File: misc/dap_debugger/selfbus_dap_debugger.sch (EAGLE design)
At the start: 60 parts, among them CON1 MICRO-B_U254-051N-4BH806, CON2 SHF-105-01-X-D-TH, CON3 SHF-105-01-X-D-TH, CON4 SAMTEC-LTMM-105-02-T-D, IC1 74LVC1T45GW, IC2 74LVC2G07GV, IC3 74LVC2T45DC, IC4 74LVC2T45DC, SW1 BOOT, SW2 RESET, SW3 XKB7070-Z, U1 STM32F042FX, U2 AP2112K-3.3TRG1, U3 AP2331TDW

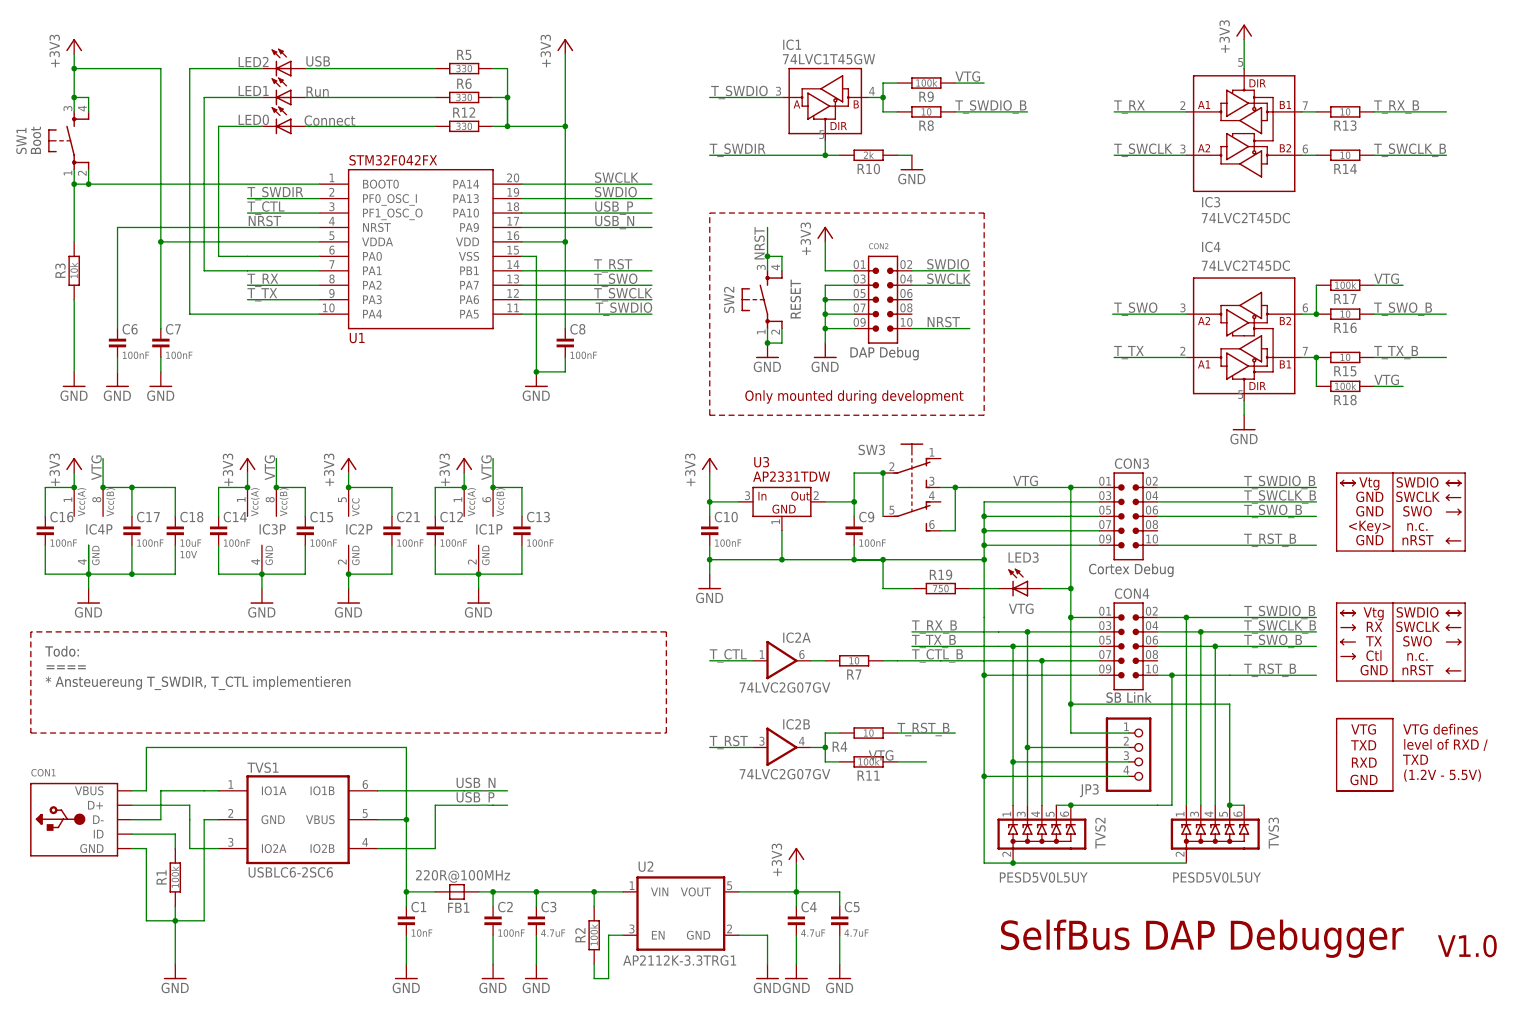
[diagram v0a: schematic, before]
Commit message: Switched from Micro-USB to USB-C
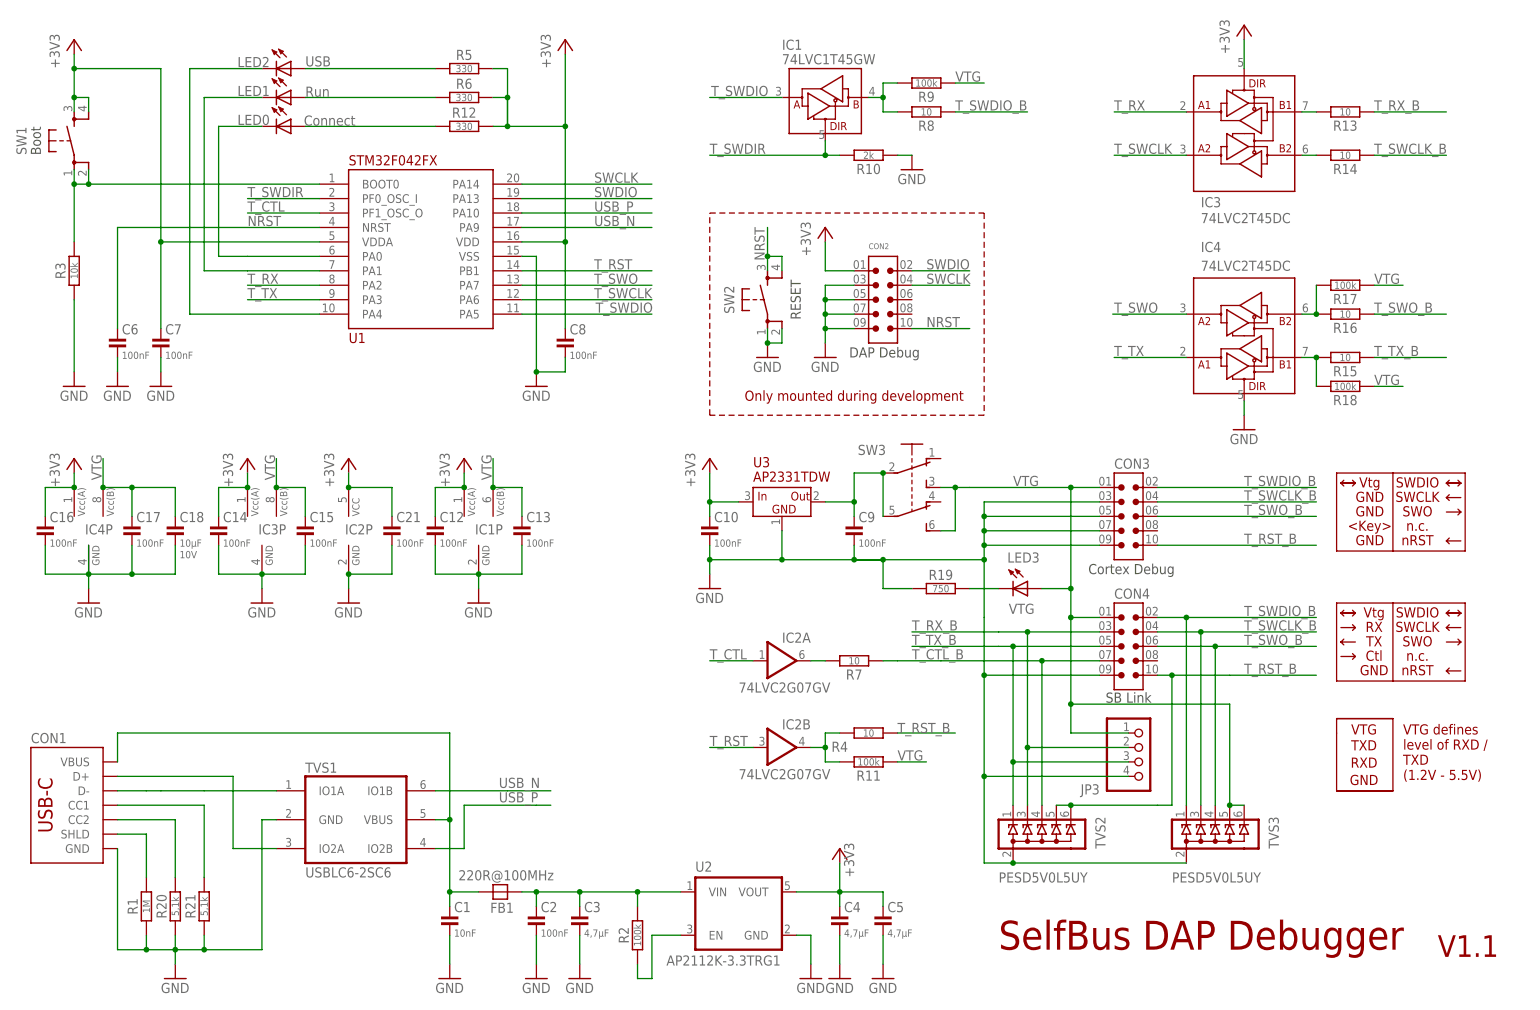
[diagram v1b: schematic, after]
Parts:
- added R20, R21: 5,1k, MyRCL:R-EU_R0805
- C18: value 10uF -> 10µF
- C3, C4, C5: value 4.7uF -> 4,7µF
- CON1: value MICRO-B_U254-051N-4BH806 -> XKB U262-161N-4BVC11; device MyCon-USB:MICRO-B_U254-051N-4BH806 -> MyCon-USB:USB_C_2-LAYER_PADS; LCSC# C319170 -> (none); LSSC# (none) -> C319148
- R1: value 100k -> 1M
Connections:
- net N$4 renamed VBUS
- new net N$2: CON1.SHLD, R1.2
- new net N$5: CON1.CC1, R21.2
- net GND: now also R20.1, R21.1
- net N$3: now also CON1.CC2, R20.2; no longer CON1.ID, R1.2
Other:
- note added: "V1.1"
- note removed: "Todo: ==== * Ansteuereung T_SWDIR, T_CTL implementieren"
- note removed: "V1.0"
- moved on the sheet: C1, C2, C3, C4, C5, FB1, R1, R2, TVS1, U2

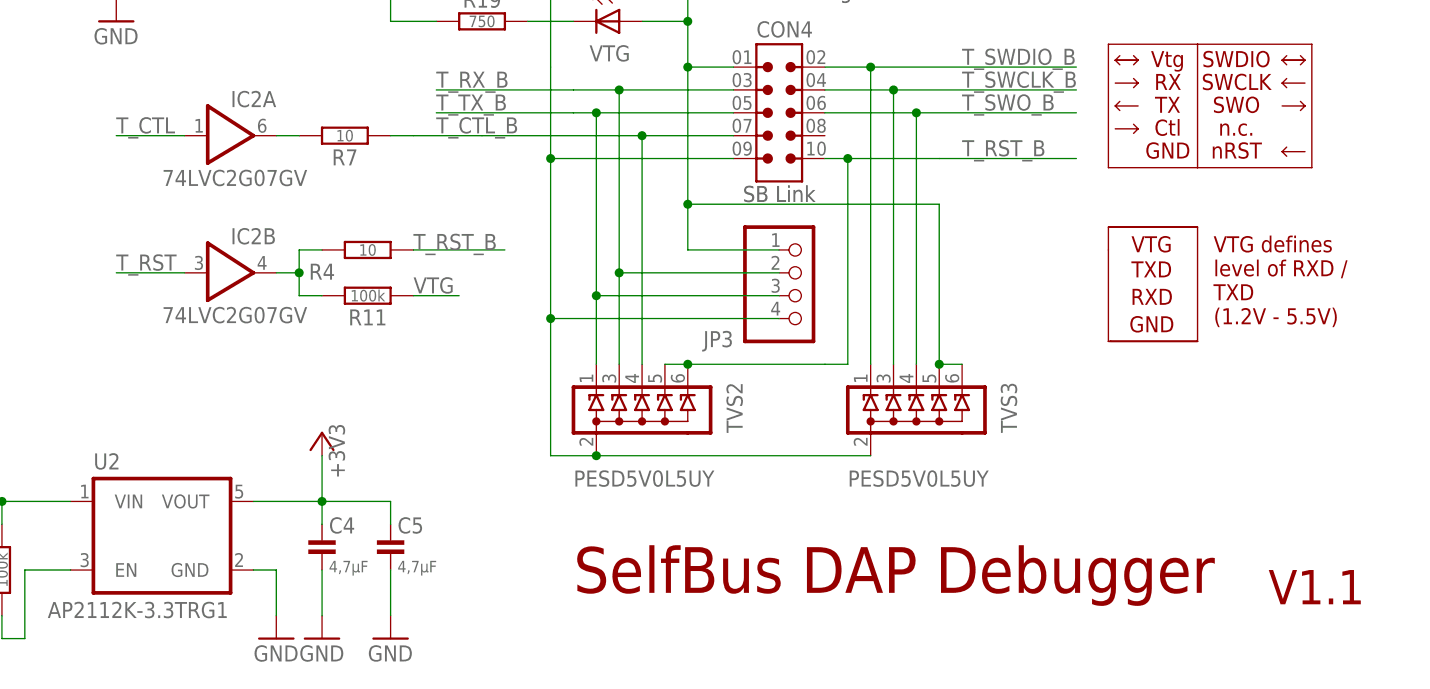
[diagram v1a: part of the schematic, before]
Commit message: IC2 package switched to SOT363/SC70
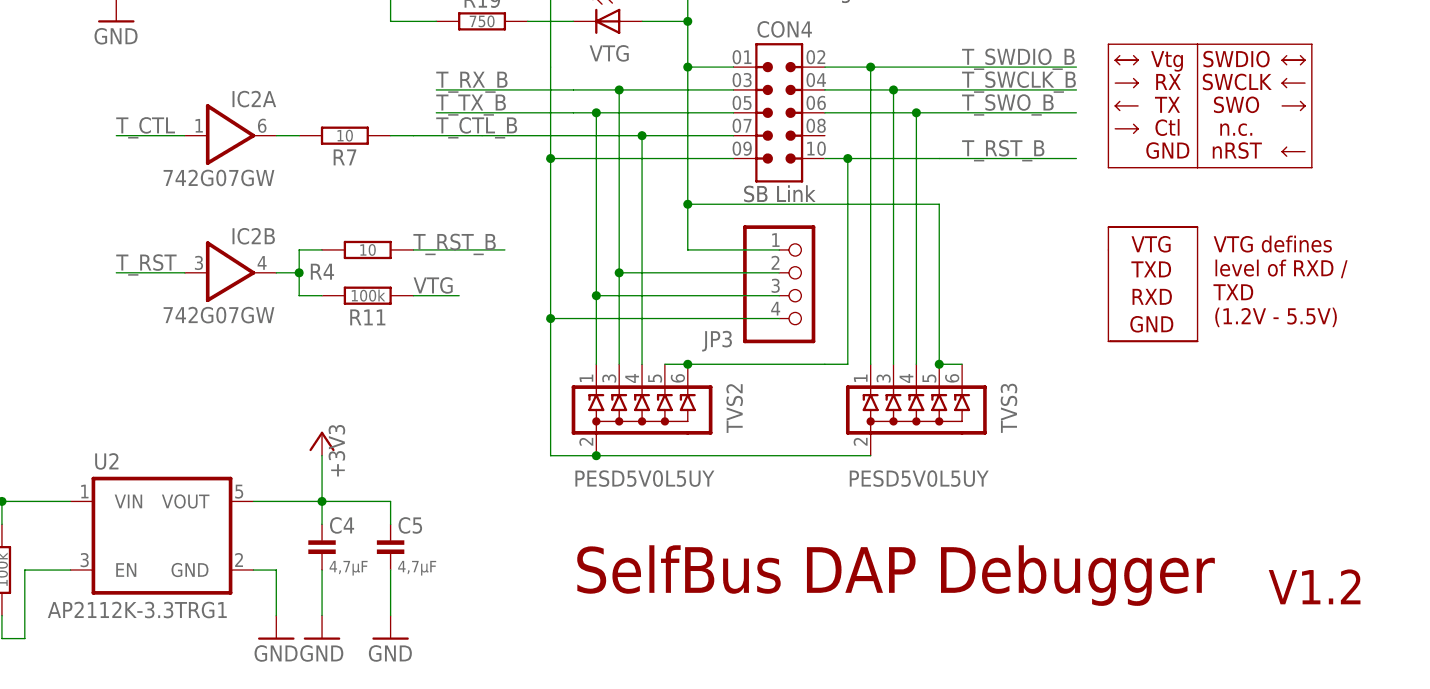
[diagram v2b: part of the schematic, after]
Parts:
- IC2: value 74LVC2G07GV -> 742G07GW; device MyIC-Logic:74LVC2G07GV -> MyIC-Logic:742G07GW; LCSC# C548568 -> C24478; MOUSER# 771-LVC2G07GV125 -> (none); PART# 74LVC2G07GV,125 -> 74LVC2G07GW,125
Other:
- note added: "V1.2"
- note removed: "V1.1"
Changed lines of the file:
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@@
 </part>
 <part name="TVS3" library="MyESD" deviceset="PESD5V0L5" device="UY" package3d_urn="urn:adsk.eagle:package:29757/2"/>
-<part name="IC2" library="MyIC-Logic" deviceset="74*2G07" device="GV" package3d_urn="urn:adsk.eagle:package:16490/2" technology="LVC">
-<attribute name="LCSC#" value="C548568"/>
-<attribute name="MOUSER#" value="771-LVC2G07GV125"/>
-<attribute name="PART#" value="74LVC2G07GV,125"/>
+<part name="IC2" library="MyIC-Logic" deviceset="74*2G07" device="GW" package3d_urn="urn:adsk.eagle:package:29757/2" value="742G07GW">
+<attribute name="LCSC#" value="C24478"/>
+<attribute name="PART#" value="74LVC2G07GW,125"/>
 <attribute name="PART_MFR" value="NXP"/>
 </part>
@@
 <plain>
 <text x="175.26" y="12.7" size="5.08" layer="94">SelfBus DAP Debugger</text>
-<text x="252.476" y="11.43" size="3.81" layer="94">V1.1</text>
+<text x="252.476" y="11.43" size="3.81" layer="94">V1.2</text>
 <text x="155.194" y="116.84" size="1.778" layer="97" align="bottom-center">DAP Debug</text>
 <text x="149.86" y="109.22" size="1.778" layer="94" align="bottom-center">Only mounted during development</text>
@@
 <attribute name="VALUE" x="129.54" y="57.912" size="1.778" layer="96"/>
 <attribute name="PART#" x="137.16" y="63.5" size="1.778" layer="96" display="off"/>
-<attribute name="MOUSER#" x="137.16" y="63.5" size="1.778" layer="96" display="off"/>
 <attribute name="LCSC#" x="137.16" y="63.5" size="1.778" layer="96" display="off"/>
 <attribute name="PART_MFR" x="137.16" y="63.5" size="1.778" layer="96" display="off"/>
